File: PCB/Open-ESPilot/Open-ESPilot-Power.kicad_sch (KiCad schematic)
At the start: 29 parts, among them J15 VOUT, J2 VIN, J3 GND, M1 Clone "MP1584" module, Q3 AO3401A, U2 AMS1117-3.3, U3 INA219AxD, U8 AMS1117-3.3

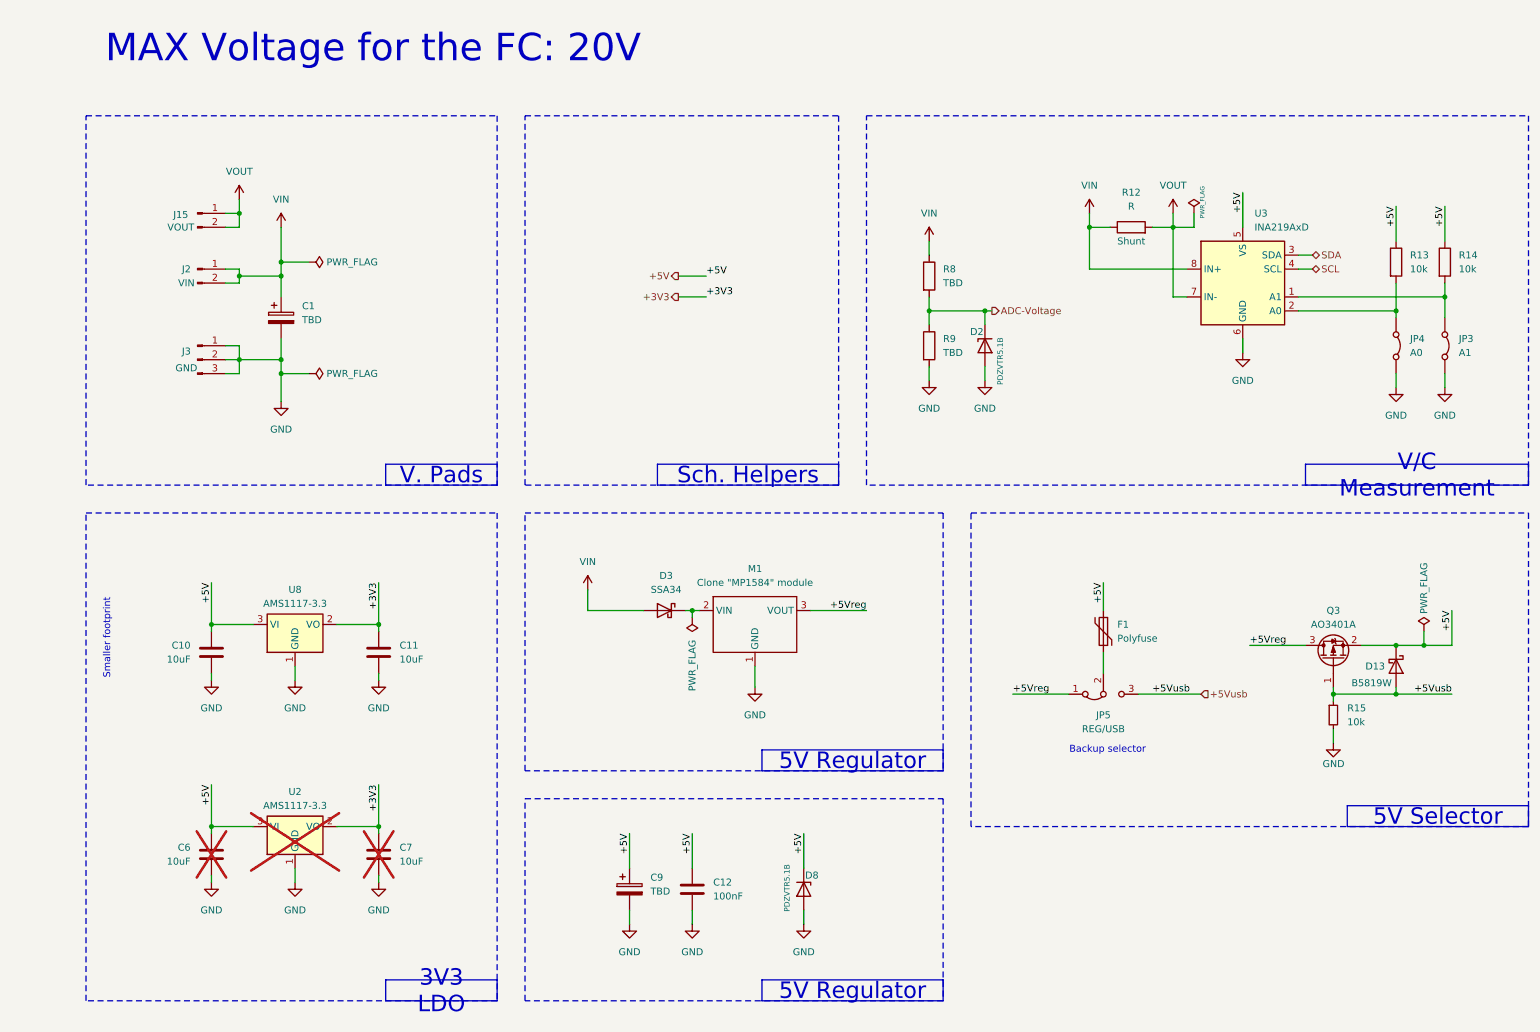
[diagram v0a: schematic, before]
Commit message: Added new footprints for power pads and added decoupling capacitors.
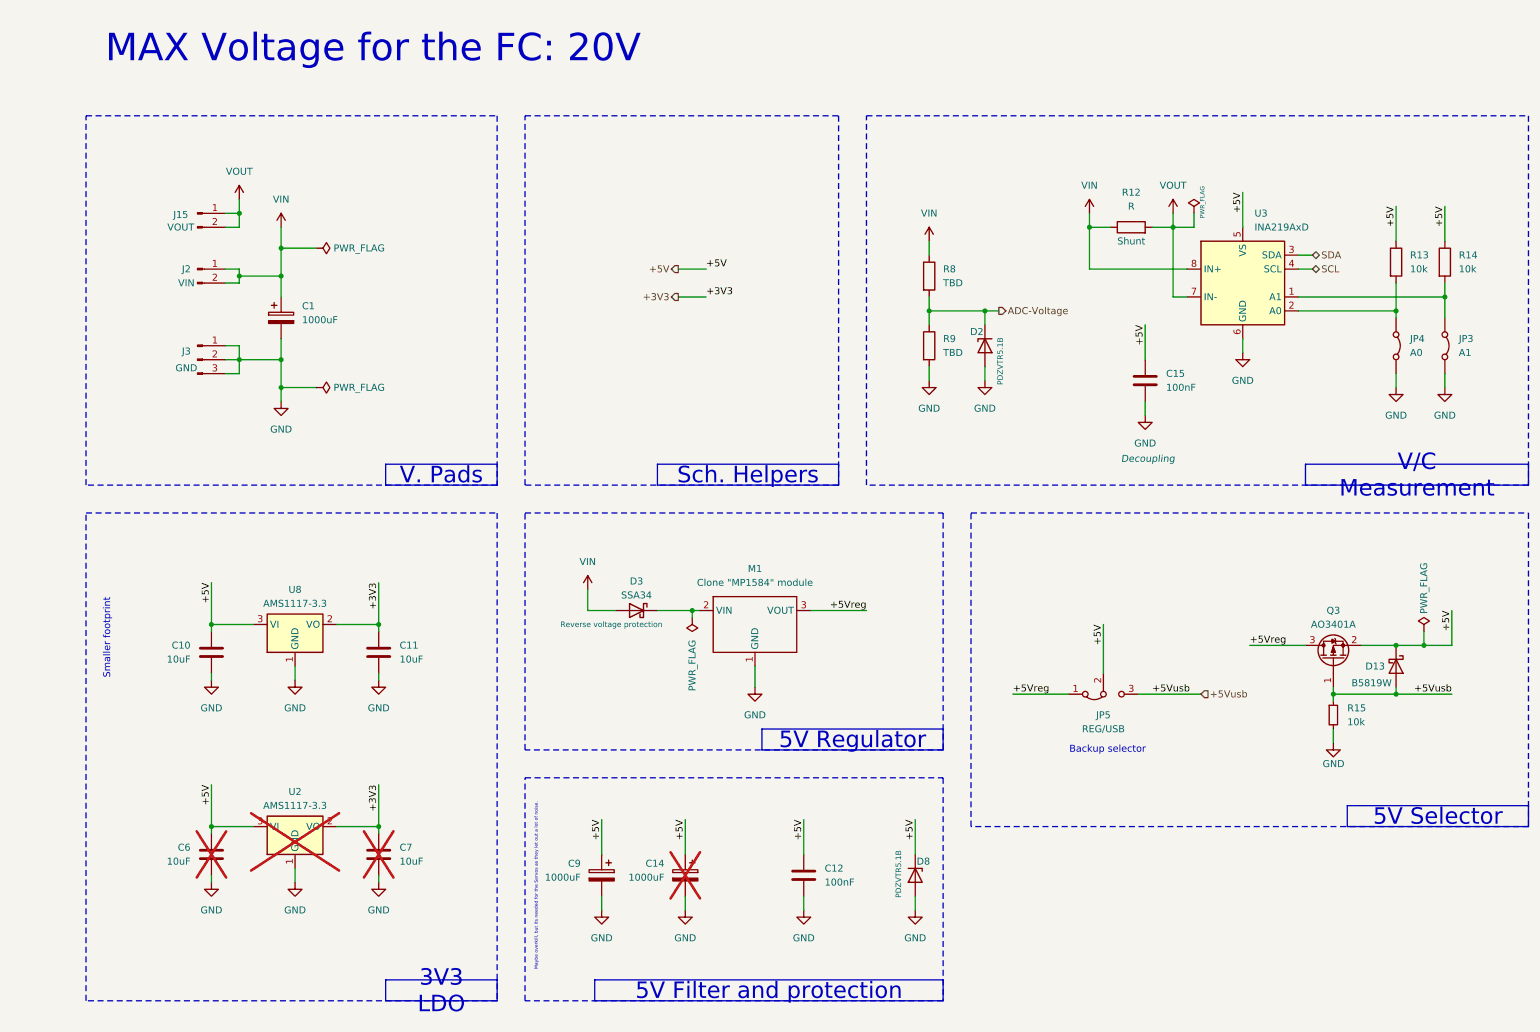
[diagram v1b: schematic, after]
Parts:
- removed F1: Polyfuse, symbol Device:Polyfuse
- added C14: 1000uF, Capacitor_THT:CP_Radial_D10.0mm_P5.00mm_P7.50mm, symbol Device:C_Polarized
- added C15: 100nF, Capacitor_SMD:C_0805_2012Metric_Pad1.18x1.45mm_HandSolder, symbol Device:C
- C1: value TBD -> 1000uF; footprint (none) -> Capacitor_THT:CP_Radial_D10.0mm_P5.00mm_P7.50mm; LCSC (none) -> C398835
- C9: value TBD -> 1000uF; footprint (none) -> Capacitor_SMD:CP_Elec_8x10; LCSC (none) -> C311227
- D3: Function (none) -> Reverse voltage protection
- J15, J2: footprint (none) -> Power Pads:PP_02x
- J3: footprint (none) -> Power Pads:PP_03x
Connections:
- net +5V: now also JP5.2 (C), C14.1, C15.1
- net GND: now also C14.2, C15.2
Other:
- note added: "Maybe overkill, but its needed for the Servos as they let out a lot of noise."
- moved on the sheet: C12, C9, D3, D8

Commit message: Completed the INA219 current sensor schematic. Changed the I2C pullups for a value thats common on board.
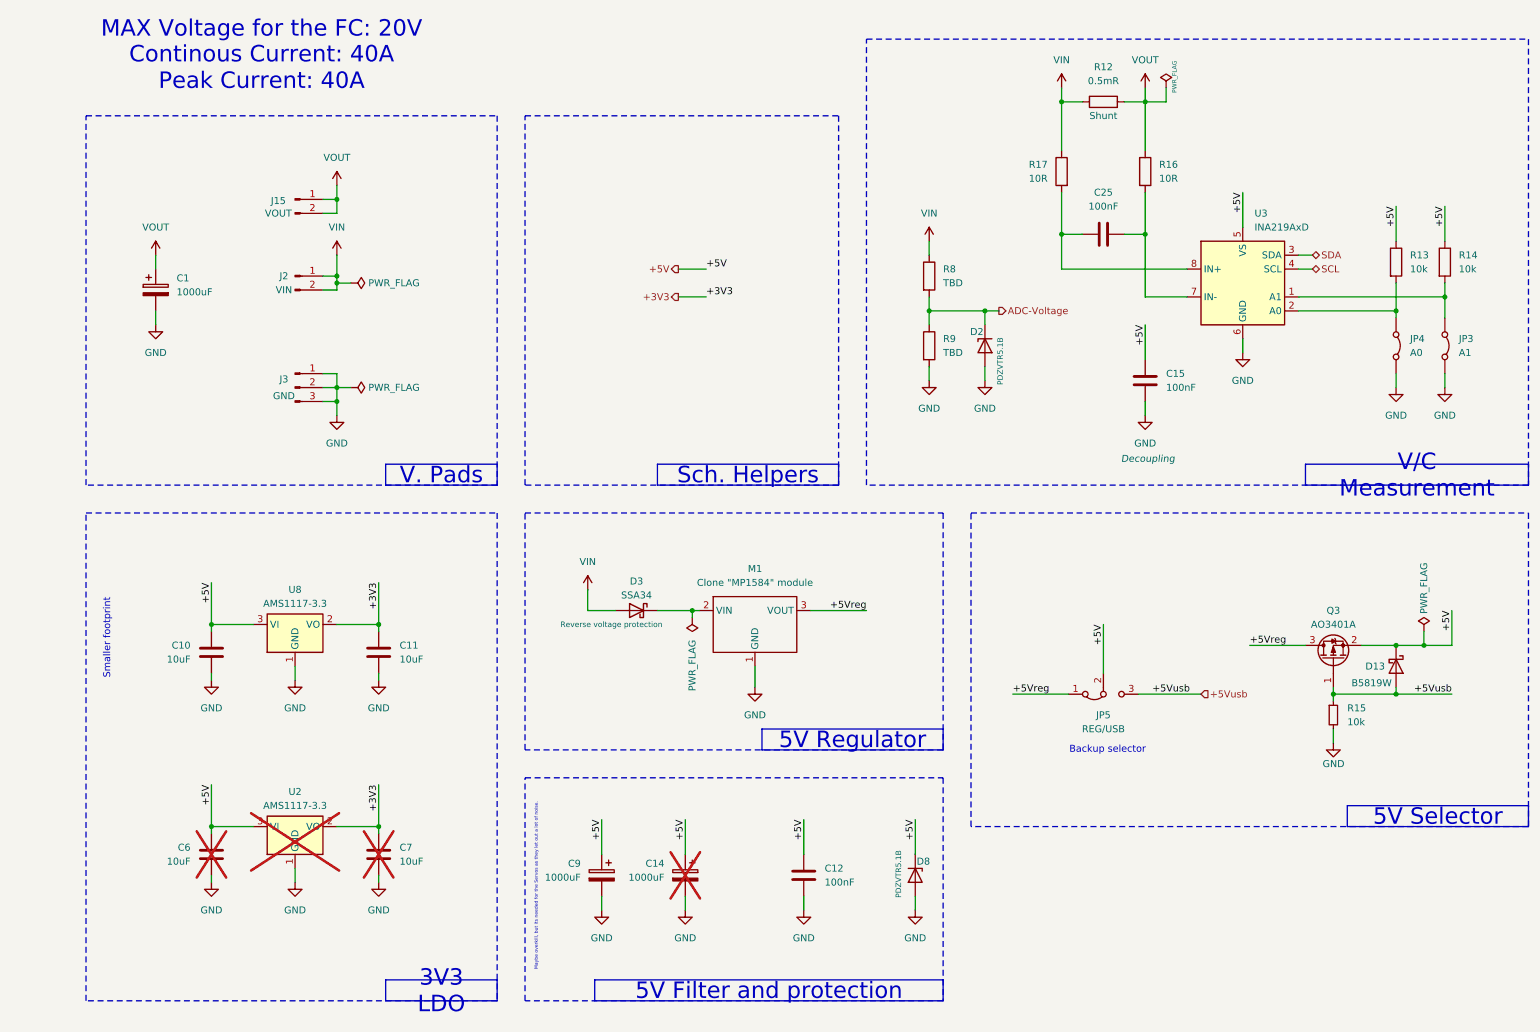
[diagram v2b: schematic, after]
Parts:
- added C25: 100nF, Capacitor_SMD:C_0805_2012Metric_Pad1.18x1.45mm_HandSolder, symbol Device:C
- added R16, R17: 10R, Resistor_SMD:R_0805_2012Metric_Pad1.20x1.40mm_HandSolder, symbol Device:R
- R12: value R -> 0.5mR; footprint (none) -> Resistor_SMD:R_2512_6332Metric_Pad1.40x3.35mm_HandSolder; Alternative (none) -> C312481; LCSC (none) -> C37635712; Maybe https://lcsc.com/product-detail/Chip-Resistor-Surface-Mount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 -> (none)
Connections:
- net VIN: now also R17.1; no longer C1.1, U3.8 (IN+)
- net VOUT: now also C1.1, R16.1; no longer U3.7 (IN-)
- new net: C25.2, R16.2, U3.7 (IN-)
- new net: C25.1, R17.2, U3.8 (IN+)
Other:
- note added: "Continous Current: 40A Peak Current: 40A"
- moved on the sheet: C1, J15, J2, J3, R12

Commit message: Adjusted the Power schematic.
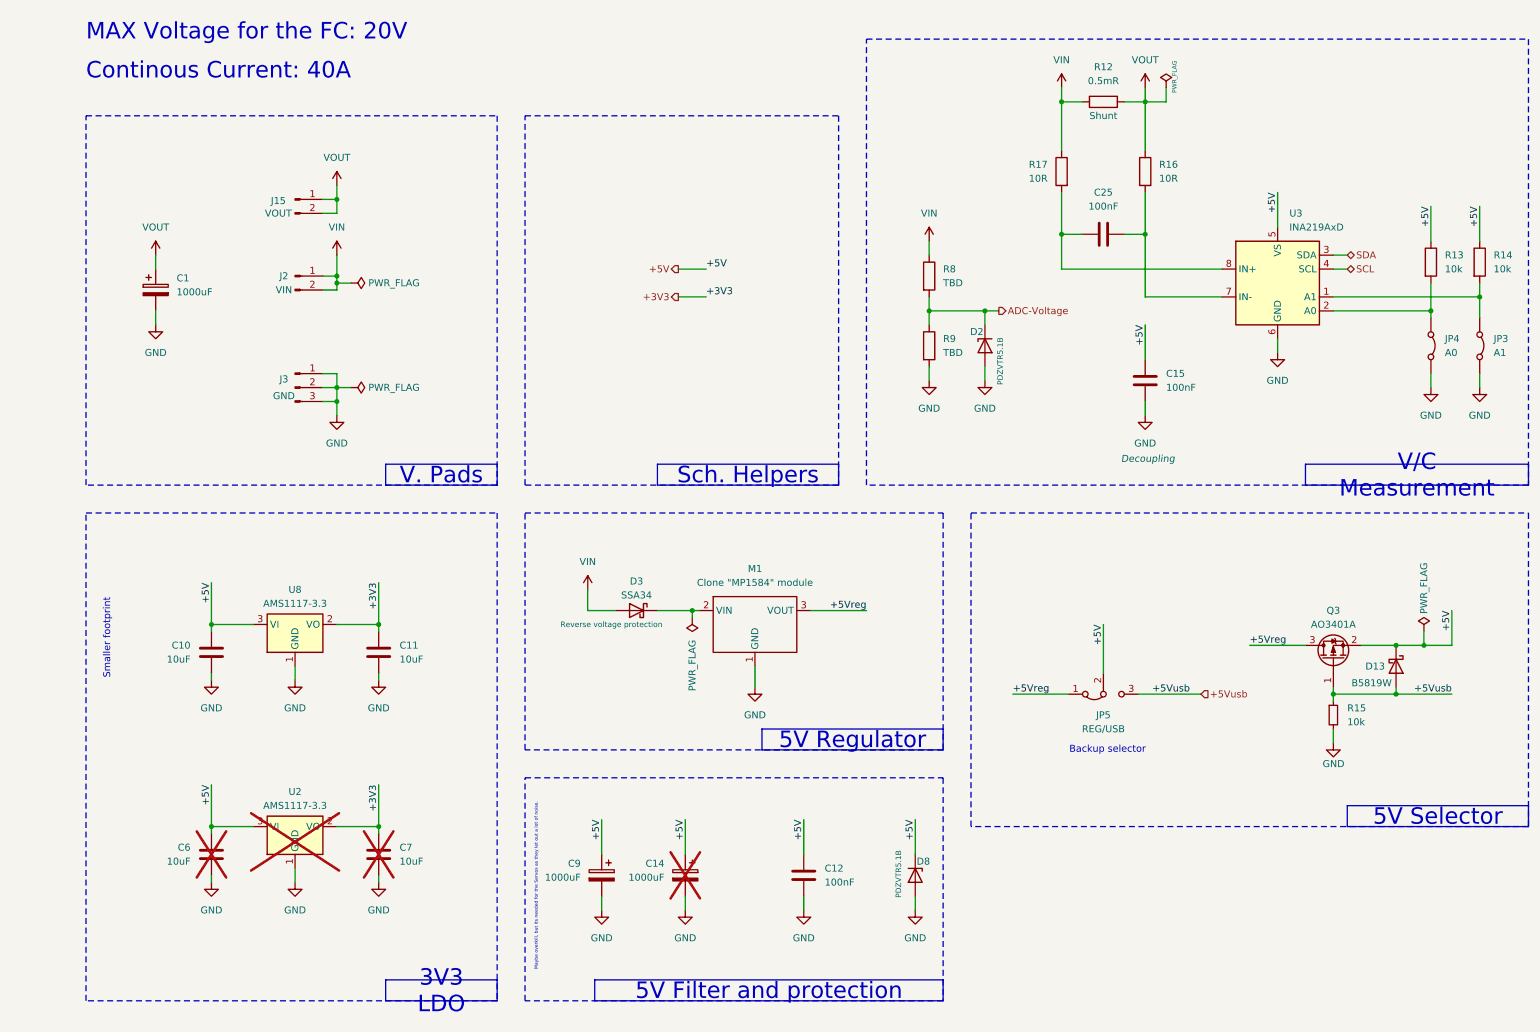
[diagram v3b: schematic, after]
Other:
- note added: "Continous Current: 40A"
- note removed: "Continous Current: 40A Peak Current: 40A"
- moved on the sheet: JP3, JP4, R13, R14, U3

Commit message: Reanotated Schematic.
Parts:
- C6: renamed from C10; value 10uF -> 22uF
- C7: renamed from C6; value 10uF -> 22uF
- C8: renamed from C11; value 10uF -> 22uF
- C9: renamed from C7; value 10uF -> 22uF
- renumbered C9 to C10, C14 to C11, C25 to C13, C15 to C14, C1 to C5, D3 to D1, D8 to D2, D2 to D3, D13 to D4, J15 to J2, J2 to J3, J3 to J4, JP5 to JP1, JP4 to JP2, Q3 to Q1, R15 to R10, R13 to R11, R14 to R12, R8 to R5, R9 to R6, R17 to R7, R12 to R8, R16 to R9, U8 to U2, U2 to U3, U3 to U4

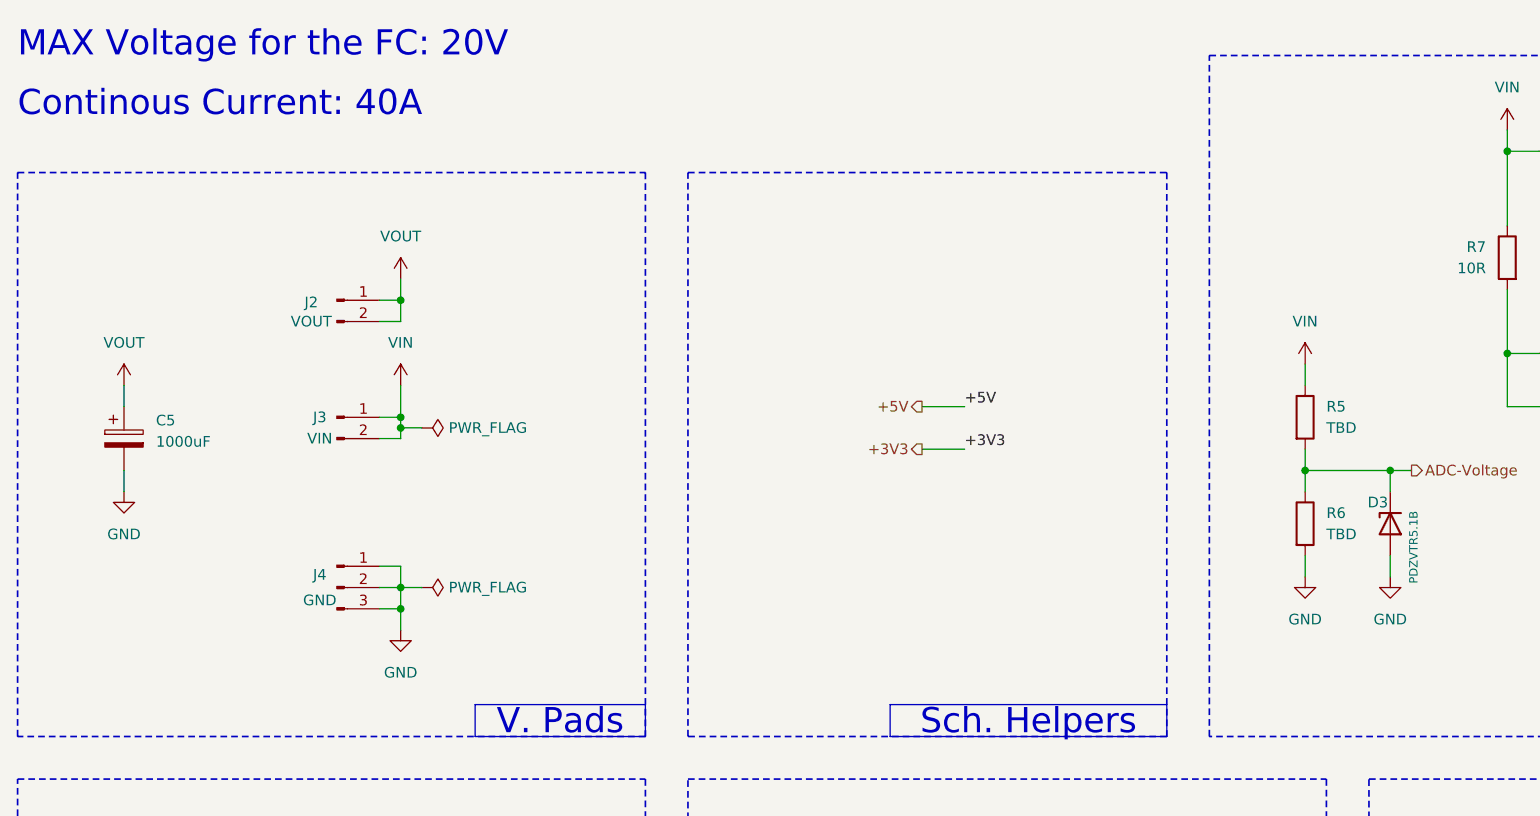
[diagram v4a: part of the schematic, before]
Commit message: Decided on voltage divider.
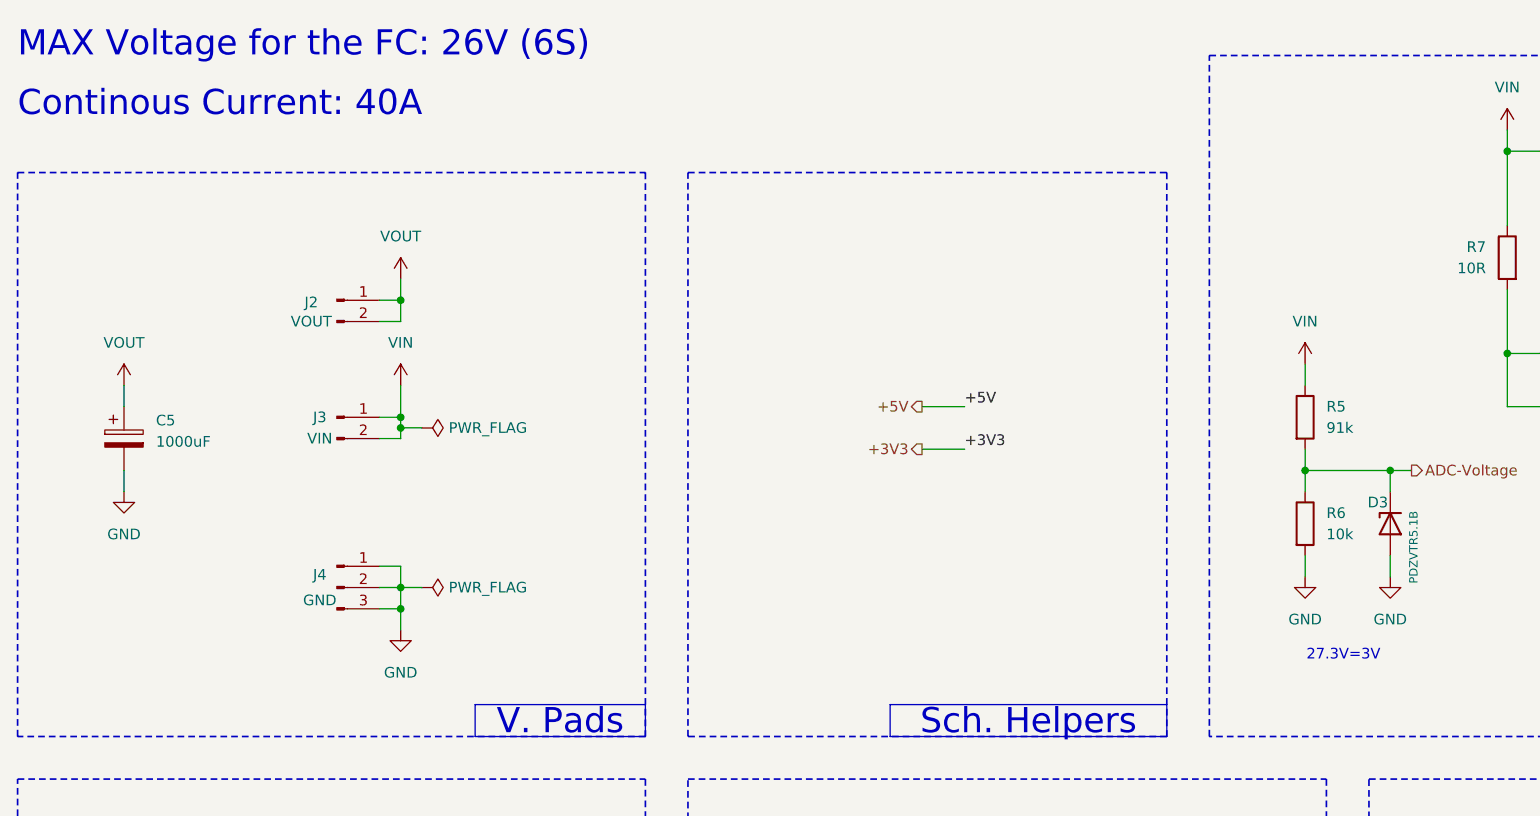
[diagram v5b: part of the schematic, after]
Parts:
- R5: value TBD -> 91k
- R6: value TBD -> 10k
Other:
- note added: "27.3V=3V"
- note added: "MAX Voltage for the FC: 26V (6S)"
- note removed: "MAX Voltage for the FC: 20V"
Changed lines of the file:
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@@
 		)
 	)
-	(text "MAX Voltage for the FC: 20V"
+	(text "MAX Voltage for the FC: 26V (6S)"
 		(exclude_from_sim no)
 		(at 16.51 16.51 0)
@@
 		)
 	)
+	(text "27.3V=3V"
+		(exclude_from_sim no)
+		(at 174.752 89.408 0)
+		(effects
+			(font
+				(size 1.27 1.27)
+			)
+		)
+	)
 	(text_box "V. Pads"
 		(exclude_from_sim no)
@@
 			)
 		)
-		(property "Value" "TBD"
+		(property "Value" "91k"
 			(at 172.72 62.2299 0)
 			(effects
@@
 			)
 		)
-		(property "Value" "TBD"
+		(property "Value" "10k"
 			(at 172.72 74.9299 0)
 			(effects

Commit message: PCB init.
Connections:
- net VIN: no longer D1.2 (A), R5.1
- net VOUT: now also D1.2 (A), R5.1
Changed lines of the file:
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@@
 			)
 		)
-		(property "Value" "VIN"
+		(property "Value" "VOUT"
 			(at 170.18 49.53 0)
 			(effects
@@
 			)
 		)
-		(property "Value" "VIN"
+		(property "Value" "VOUT"
 			(at 107.95 113.03 0)
 			(effects

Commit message: Started routing. I have few things there. Fixed schematic.
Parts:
- C5: footprint Capacitor_THT:CP_Radial_D10.0mm_P5.00mm_P7.50mm -> Capacitor_THT:CP_Radial_D10.0mm_P5.00mm
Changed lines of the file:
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@@
 			)
 		)
-		(property "Footprint" "Capacitor_THT:CP_Radial_D10.0mm_P5.00mm_P7.50mm"
+		(property "Footprint" "Capacitor_THT:CP_Radial_D10.0mm_P5.00mm"
 			(at 30.1752 67.31 0)
 			(effects
